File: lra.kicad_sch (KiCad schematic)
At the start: 48 parts, among them J10 Conn_01x08_Female, J12 Conn_01x08_Female, U10 DRV2605LDGS, U11 DRV2605LDGS, U12 DRV2605LDGS, U13 DRV2605LDGS, U14 DRV2605LDGS, U15 DRV2605LDGS, U7 TCA9548ARGER, U8 DRV2605LDGS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

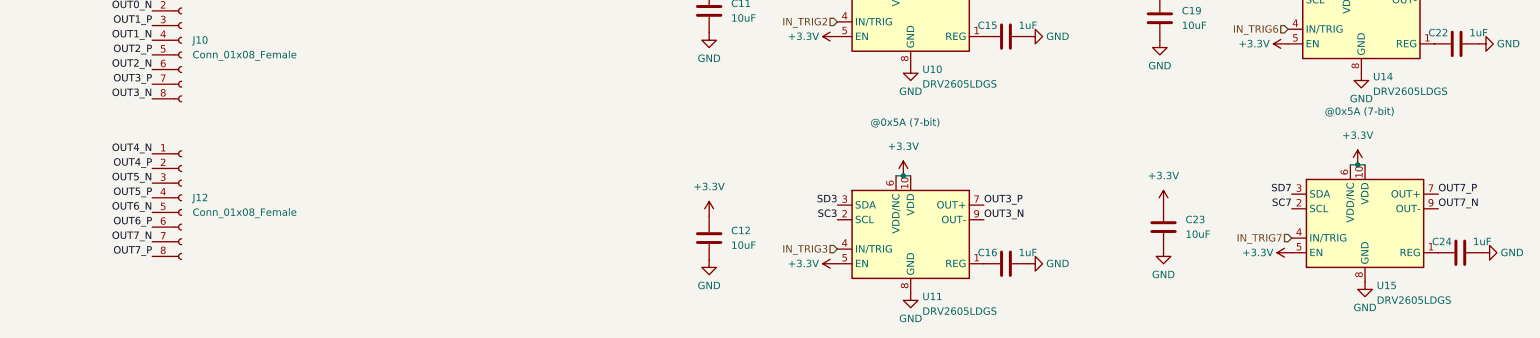
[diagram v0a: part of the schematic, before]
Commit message: Routing done, silkscreen cleaning, update README, remove old files
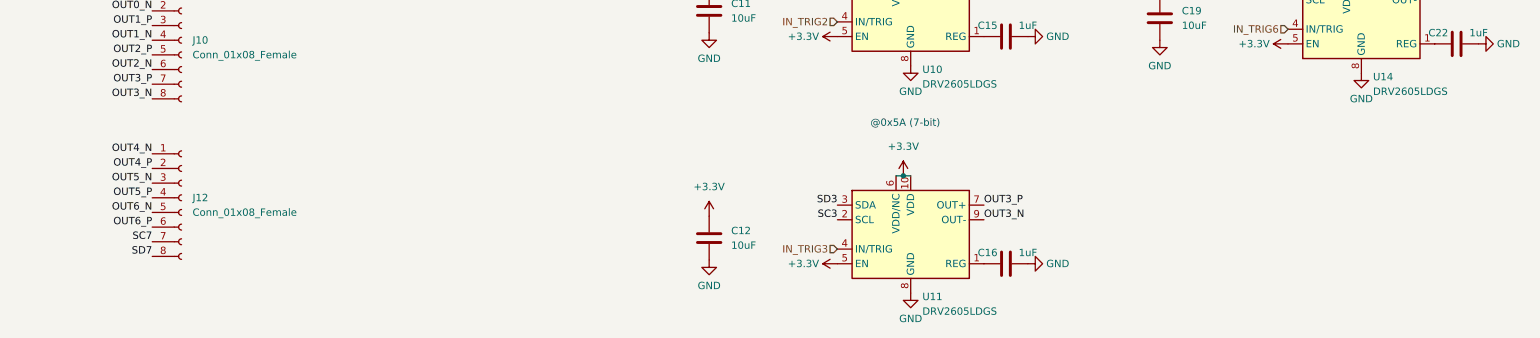
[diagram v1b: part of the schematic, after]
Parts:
- removed C23: 10uF, Capacitor_SMD:C_0402_1005Metric, symbol Device:C
- removed C24: 1uF, Capacitor_SMD:C_0402_1005Metric, symbol Device:C
- removed U15: DRV2605LDGS, Package_SO:VSSOP-10_3x3mm_P0.5mm, symbol Driver_Haptic:DRV2605LDGS
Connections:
- net OUT7_N is gone; now on net SC7: J12.7 (Pin_7)
- net OUT7_P is gone; now on net SD7: J12.8 (Pin_8)
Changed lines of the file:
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@@
 (kicad_sch (version 20211123) (generator eeschema)
   (paper "A4")
-  (junction (at 255.27 135.89) (diameter 0) (color 0 0 0 0)
-  )
   (junction (at 175.895 61.595) (diameter 0) (color 0 0 0 0)
   )
@@
     (stroke (width 0) (type default) (color 0 0 0 0))
   )
-  (wire (pts (xy 254 135.89) (xy 255.27 135.89))
-    (stroke (width 0) (type default) (color 0 0 0 0))
-  )
   (wire (pts (xy 36.195 53.975) (xy 40.005 53.975))
     (stroke (width 0) (type default) (color 0 0 0 0))
@@
     (stroke (width 0) (type default) (color 0 0 0 0))
   )
-  (wire (pts (xy 255.27 135.89) (xy 256.54 135.89))
-    (stroke (width 0) (type default) (color 0 0 0 0))
-  )
   (wire (pts (xy 175.895 61.595) (xy 177.165 61.595))
     (stroke (width 0) (type default) (color 0 0 0 0))
@@
     (stroke (width 0) (type default) (color 0 0 0 0))
   )
-  (text "@0x5A (7-bit)" (at 249.555 127.635 0)
-    (effects (font (size 1.27 1.27)) (justify left bottom))
-  )
   (text "@0x5A (7-bit)" (at 248.285 54.61 0)
     (effects (font (size 1.27 1.27)) (justify left bottom))
@@
     (effects (font (size 1.27 1.27)) (justify left bottom))
   )
-  (label "SC7" (at 243.84 143.51 180)
+  (label "SC7" (at 46.355 149.225 180)
     (effects (font (size 1.27 1.27)) (justify right bottom))
   )
@@
     (effects (font (size 1.27 1.27)) (justify left bottom))
   )
-  (label "OUT7_N" (at 46.355 149.225 180)
-    (effects (font (size 1.27 1.27)) (justify right bottom))
-  )
   (label "SD1" (at 67.945 36.195 0)
     (effects (font (size 1.27 1.27)) (justify left bottom))
@@
     (effects (font (size 1.27 1.27)) (justify left bottom))
   )
-  (label "OUT7_N" (at 269.24 143.51 0)
-    (effects (font (size 1.27 1.27)) (justify left bottom))
-  )
   (label "OUT6_N" (at 46.355 144.145 180)
     (effects (font (size 1.27 1.27)) (justify right bottom))
@@
     (effects (font (size 1.27 1.27)) (justify left bottom))
   )
-  (label "OUT7_P" (at 269.24 140.97 0)
-    (effects (font (size 1.27 1.27)) (justify left bottom))
-  )
   (label "OUT5_N" (at 46.355 139.065 180)
     (effects (font (size 1.27 1.27)) (justify right bottom))
@@
     (effects (font (size 1.27 1.27)) (justify left bottom))
   )
-  (label "SD7" (at 243.84 140.97 180)
+  (label "SD7" (at 46.355 151.765 180)
     (effects (font (size 1.27 1.27)) (justify right bottom))
   )
@@
     (effects (font (size 1.27 1.27)) (justify right bottom))
   )
-  (label "OUT7_P" (at 46.355 151.765 180)
-    (effects (font (size 1.27 1.27)) (justify right bottom))
-  )
   (label "SD7" (at 67.945 51.435 0)
     (effects (font (size 1.27 1.27)) (justify left bottom))
@@
   (label "OUT2_N" (at 46.355 119.38 180)
     (effects (font (size 1.27 1.27)) (justify right bottom))
-  )
-  (hierarchical_label "IN_TRIG7" (shape input) (at 243.84 148.59 180)
-    (effects (font (size 1.27 1.27)) (justify right))
   )
   (hierarchical_label "IN_TRIG3" (shape input) (at 165.1 150.495 180)
@@
     (pin "1")
   )
-  (symbol (lib_id "Device:C") (at 273.05 151.13 90) (unit 1)
-    (in_bom yes) (on_board yes)
-    (property "Reference" "C24" (id 0) (at 269.875 149.225 90))
-    (property "Value" "1uF" (id 1) (at 276.86 149.225 90))
-    (property "Footprint" "Capacitor_SMD:C_0402_1005Metric" (id 2) (at 276.86 150.1648 0)
-      (effects (font (size 1.27 1.27)) hide)
-    )
-    (property "Datasheet" "~" (id 3) (at 273.05 151.13 0)
-      (effects (font (size 1.27 1.27)) hide)
-    )
-    (pin "1")
-    (pin "2")
-  )
   (symbol (lib_id "power:GND") (at 197.485 76.835 90) (unit 1)
     (in_bom yes) (on_board yes) (fields_autoplaced)
@@
     (pin "1")
   )
-  (symbol (lib_id "power:GND") (at 256.54 156.21 0) (unit 1)
-    (in_bom yes) (on_board yes) (fields_autoplaced)
-    (property "Reference" "#PWR0217" (id 0) (at 256.54 162.56 0)
-      (effects (font (size 1.27 1.27)) hide)
-    )
-    (property "Value" "GND" (id 1) (at 256.54 160.655 0))
-    (property "Footprint" "" (id 2) (at 256.54 156.21 0)
-      (effects (font (size 1.27 1.27)) hide)
-    )
-    (property "Datasheet" "" (id 3) (at 256.54 156.21 0)
-      (effects (font (size 1.27 1.27)) hide)
-    )
-    (pin "1")
-  )
   (symbol (lib_id "power:+3.3V") (at 220.345 33.02 0) (unit 1)
     (in_bom yes) (on_board yes) (fields_autoplaced)
@@
     (pin "1")
   )
-  (symbol (lib_id "power:+3.3V") (at 221.615 142.875 0) (unit 1)
-    (in_bom yes) (on_board yes) (fields_autoplaced)
-    (property "Reference" "#PWR0222" (id 0) (at 221.615 146.685 0)
-      (effects (font (size 1.27 1.27)) hide)
-    )
-    (property "Value" "+3.3V" (id 1) (at 221.615 137.795 0))
-    (property "Footprint" "" (id 2) (at 221.615 142.875 0)
-      (effects (font (size 1.27 1.27)) hide)
-    )
-    (property "Datasheet" "" (id 3) (at 221.615 142.875 0)
-      (effects (font (size 1.27 1.27)) hide)
-    )
-    (pin "1")
-  )
   (symbol (lib_id "Device:R") (at 43.815 53.975 90) (unit 1)
     (in_bom yes) (on_board yes)
@@
     )
     (property "Datasheet" "" (id 3) (at 93.345 48.26 0)
-      (effects (font (size 1.27 1.27)) hide)
-    )
-    (pin "1")
-  )
-  (symbol (lib_id "power:+3.3V") (at 255.27 135.89 0) (unit 1)
-    (in_bom yes) (on_board yes) (fields_autoplaced)
-    (property "Reference" "#PWR0219" (id 0) (at 255.27 139.7 0)
-      (effects (font (size 1.27 1.27)) hide)
-    )
-    (property "Value" "+3.3V" (id 1) (at 255.27 130.81 0))
-    (property "Footprint" "" (id 2) (at 255.27 135.89 0)
-      (effects (font (size 1.27 1.27)) hide)
-    )
-    (property "Datasheet" "" (id 3) (at 255.27 135.89 0)
       (effects (font (size 1.27 1.27)) hide)
     )
@@
     (pin "1")
   )
-  (symbol (lib_id "power:GND") (at 276.86 151.13 90) (unit 1)
-    (in_bom yes) (on_board yes) (fields_autoplaced)
-    (property "Reference" "#PWR0218" (id 0) (at 283.21 151.13 0)
-      (effects (font (size 1.27 1.27)) hide)
-    )
-    (property "Value" "GND" (id 1) (at 280.035 151.1299 90)
-      (effects (font (size 1.27 1.27)) (justify right))
-    )
-    (property "Footprint" "" (id 2) (at 276.86 151.13 0)
-      (effects (font (size 1.27 1.27)) hide)
-    )
-    (property "Datasheet" "" (id 3) (at 276.86 151.13 0)
-      (effects (font (size 1.27 1.27)) hide)
-    )
-    (pin "1")
-  )
   (symbol (lib_id "power:GND") (at 255.27 46.355 0) (unit 1)
     (in_bom yes) (on_board yes) (fields_autoplaced)
@@
     (pin "1")
   )
-  (symbol (lib_id "Device:C") (at 221.615 146.685 0) (unit 1)
-    (in_bom yes) (on_board yes) (fields_autoplaced)
-    (property "Reference" "C23" (id 0) (at 225.425 145.4149 0)
-      (effects (font (size 1.27 1.27)) (justify left))
-    )
-    (property "Value" "10uF" (id 1) (at 225.425 147.9549 0)
-      (effects (font (size 1.27 1.27)) (justify left))
-    )
-    (property "Footprint" "Capacitor_SMD:C_0402_1005Metric" (id 2) (at 222.5802 150.495 0)
-      (effects (font (size 1.27 1.27)) hide)
-    )
-    (property "Datasheet" "~" (id 3) (at 221.615 146.685 0)
-      (effects (font (size 1.27 1.27)) hide)
-    )
-    (pin "1")
-    (pin "2")
-  )
-  (symbol (lib_id "power:+3.3V") (at 243.84 151.13 90) (unit 1)
-    (in_bom yes) (on_board yes) (fields_autoplaced)
-    (property "Reference" "#PWR0221" (id 0) (at 247.65 151.13 0)
-      (effects (font (size 1.27 1.27)) hide)
-    )
-    (property "Value" "+3.3V" (id 1) (at 240.665 151.1299 90)
-      (effects (font (size 1.27 1.27)) (justify left))
-    )
-    (property "Footprint" "" (id 2) (at 243.84 151.13 0)
-      (effects (font (size 1.27 1.27)) hide)
-    )
-    (property "Datasheet" "" (id 3) (at 243.84 151.13 0)
-      (effects (font (size 1.27 1.27)) hide)
-    )
-    (pin "1")
-  )
   (symbol (lib_id "Driver_Haptic:DRV2605LDGS") (at 177.165 34.925 0) (unit 1)
     (in_bom yes) (on_board yes) (fields_autoplaced)
@@
     )
     (property "Datasheet" "" (id 3) (at 57.785 23.495 0)
-      (effects (font (size 1.27 1.27)) hide)
-    )
-    (pin "1")
-  )
-  (symbol (lib_id "power:GND") (at 221.615 150.495 0) (unit 1)
-    (in_bom yes) (on_board yes) (fields_autoplaced)
-    (property "Reference" "#PWR0220" (id 0) (at 221.615 156.845 0)
-      (effects (font (size 1.27 1.27)) hide)
-    )
-    (property "Value" "GND" (id 1) (at 221.615 154.94 0))
-    (property "Footprint" "" (id 2) (at 221.615 150.495 0)
-      (effects (font (size 1.27 1.27)) hide)
-    )
-    (property "Datasheet" "" (id 3) (at 221.615 150.495 0)
       (effects (font (size 1.27 1.27)) hide)
     )
@@
     (pin "1")
   )
-  (symbol (lib_id "Driver_Haptic:DRV2605LDGS") (at 256.54 146.05 0) (unit 1)
-    (in_bom yes) (on_board yes) (fields_autoplaced)
-    (property "Reference" "U15" (id 0) (at 258.5594 156.845 0)
-      (effects (font (size 1.27 1.27)) (justify left))
-    )
-    (property "Value" "DRV2605LDGS" (id 1) (at 258.5594 159.385 0)
-      (effects (font (size 1.27 1.27)) (justify left))
-    )
-    (property "Footprint" "Package_SO:VSSOP-10_3x3mm_P0.5mm" (id 2) (at 256.54 146.05 0)
-      (effects (font (size 1.27 1.27) italic) hide)
-    )
-    (property "Datasheet" "http://www.ti.com/lit/ds/symlink/drv2605l.pdf" (id 3) (at 256.54 146.05 0)
-      (effects (font (size 1.27 1.27)) hide)
-    )
-    (property "LCSC" "C527464" (id 4) (at 256.54 146.05 0)
-      (effects (font (size 1.27 1.27)) hide)
-    )
-    (pin "1")
-    (pin "10")
-    (pin "2")
-    (pin "3")
-    (pin "4")
-    (pin "5")
-    (pin "6")
-    (pin "7")
-    (pin "8")
-    (pin "9")
-  )
   (symbol (lib_id "Driver_Haptic:DRV2605LDGS") (at 177.165 71.755 0) (unit 1)

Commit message: Small PCB layout modification, export schematic.pdf, BOM and production files for PCBWay
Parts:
- C10, C11, C12, C17, C18, C19, C5: LCSC (none) -> C315248
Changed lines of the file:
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@@
+      (effects (font (size 1.27 1.27)) hide)
+    )
+    (property "LCSC" "C315248" (id 4) (at 220.345 73.66 0)
       (effects (font (size 1.27 1.27)) hide)
     )
@@
     )
     (property "Datasheet" "~" (id 3) (at 220.345 36.83 0)
+      (effects (font (size 1.27 1.27)) hide)
+    )
+    (property "LCSC" "C315248" (id 4) (at 220.345 36.83 0)
       (effects (font (size 1.27 1.27)) hide)
     )
@@
       (effects (font (size 1.27 1.27)) hide)
     )
+    (property "LCSC" "C315248" (id 4) (at 142.875 109.22 0)
+      (effects (font (size 1.27 1.27)) hide)
+    )
     (pin "1")
     (pin "2")
@@
     )
     (property "Datasheet" "~" (id 3) (at 220.98 110.49 0)
+      (effects (font (size 1.27 1.27)) hide)
+    )
+    (property "LCSC" "C315248" (id 4) (at 220.98 110.49 0)
       (effects (font (size 1.27 1.27)) hide)
     )
@@
       (effects (font (size 1.27 1.27)) hide)
     )
+    (property "LCSC" "C315248" (id 4) (at 142.24 35.56 0)
+      (effects (font (size 1.27 1.27)) hide)
+    )
     (pin "1")
     (pin "2")
@@
     )
     (property "Datasheet" "~" (id 3) (at 142.875 148.59 0)
+      (effects (font (size 1.27 1.27)) hide)
+    )
+    (property "LCSC" "C315248" (id 4) (at 142.875 148.59 0)
       (effects (font (size 1.27 1.27)) hide)
     )
@@
       (effects (font (size 1.27 1.27)) hide)
     )
+    (property "LCSC" "C315248" (id 4) (at 142.24 72.39 0)
+      (effects (font (size 1.27 1.27)) hide)
+    )
